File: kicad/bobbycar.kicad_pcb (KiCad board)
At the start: 2 copper layers, 42 x 45 mm, 54 parts, among them J1 IO, J11 CAN2, J12 PROG, J2 IO2, J3 GAS, J4 TFT, J5 Conn_01x04, J7 BREMSE, J8 I2C, J9 CAN3, Q1 SI2301CDS-T1-GE3, U1 ESP32-WROOM-32, U2 TJA1051T-3, U3 MPM2359, U5 MPM2359

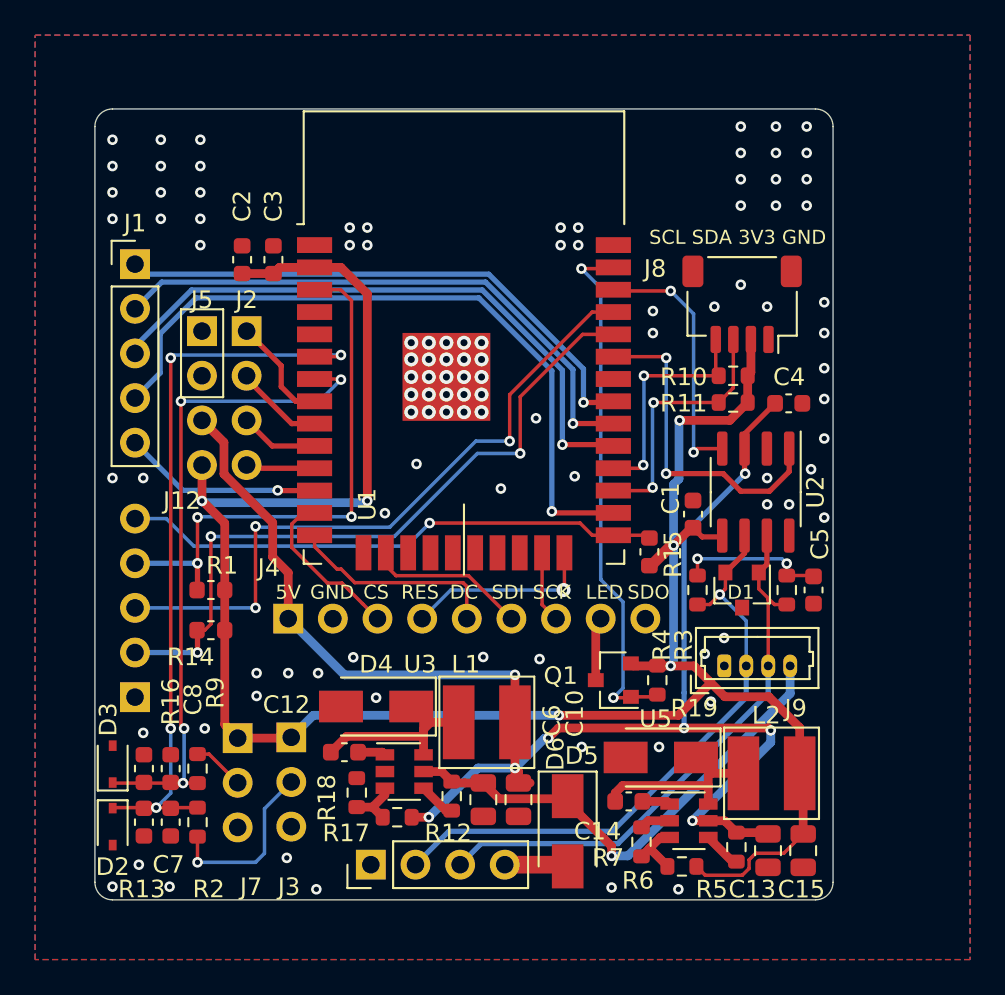
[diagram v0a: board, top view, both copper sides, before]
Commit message: changed to single 3.3V dcdc
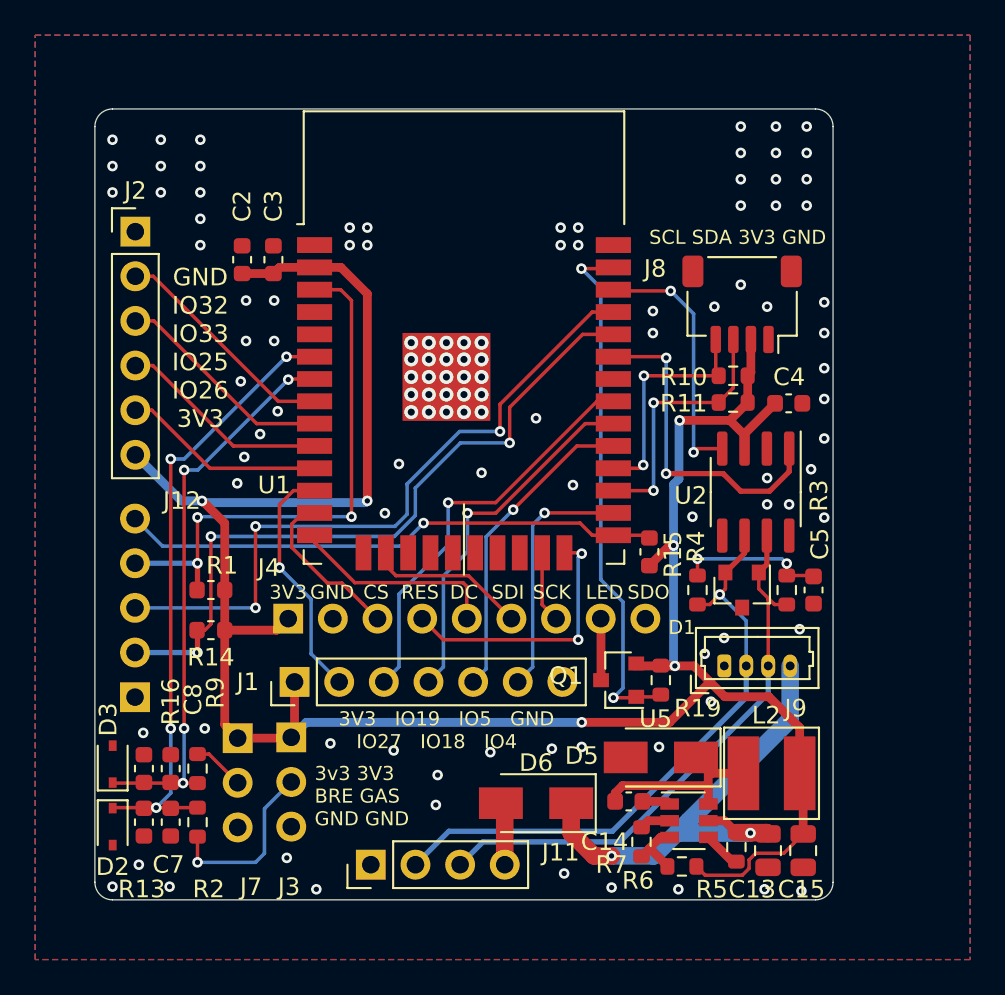
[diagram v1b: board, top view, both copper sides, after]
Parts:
- removed C1: 100n, Capacitor_SMD:C_0603_1608Metric
- removed C10, C6: 22uF, Capacitor_SMD:C_0805_2012Metric
- removed C12: 10n, Capacitor_SMD:C_0603_1608Metric
- removed D4: B230A, Diode_SMD:D_SMA
- removed J5: Conn_01x04, Connector_PinHeader_2.54mm:PinHeader_1x04_P2.54mm_Vertical
- removed L1: 4.7uH, boardcomputer:L_5040
- removed R12: 1k, Resistor_SMD:R_0603_1608Metric
- removed R17: 49.9k, Resistor_SMD:R_0603_1608Metric
- removed R18: 9.53k, Resistor_SMD:R_0603_1608Metric
- removed U3: MPM2359, Package_TO_SOT_SMD:SOT-23-6
- J1: footprint Connector_PinHeader_2.54mm:PinHeader_1x05_P2.54mm_Vertical -> Connector_PinHeader_2.54mm:PinHeader_1x07_P2.54mm_Vertical
- J2: footprint Connector_PinHeader_2.54mm:PinHeader_1x04_P2.54mm_Vertical -> Connector_PinHeader_2.54mm:PinHeader_1x06_P2.54mm_Vertical
- U2: value TJA1051T-3 -> SN65HVD231
- moved J1 25.4 mm to (106.4, 60.6), turned to 90 degrees
- moved J2 8.49 mm to (97.3, 35.0)
- moved D6 2.41 mm to (120.1, 67.5), turned to 180 degrees
- moved Q1 0.30 mm to (124.8, 60.5)
- moved R19 0.20 mm to (127.2, 60.5)
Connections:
- C13 pad 2: +5V -> 15V
- C4 pad 1: +5V -> +3V3
- J1 pad 1: IO19 -> +3V3
- J1 pad 2: IO18 -> IO27
- J1 pad 3: IO5 -> IO19
- J1 pad 4: IO4 -> IO18
- J1 pad 5: IO27 -> IO5
- J2 pad 1: IO32 -> GND
- J2 pad 2: IO33 -> IO32
- J2 pad 3: IO25 -> IO33
- J2 pad 4: IO26 -> IO25
- J4 pad 1: +5V -> +3V3
- R5 pad 2: +5V -> 15V
- U2 pad 3: +5V -> +3V3
- U2 pad 5: +3V3 -> (no net)
- U5 pad 5: +5V -> 15V
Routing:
- net +5V: track 90.2 -> 0.00 mm, vias 8 -> 0
- net IO4: track 40.6 -> 14.2 mm
- net IO5: track 35.1 -> 17.9 mm
- net IO18: track 33.0 -> 20.9 mm
- net Net-(C12-Pad1): track 10.9 -> 0.00 mm
- net +3V3: track 129.3 -> 137.9 mm
- net IO19: track 31.6 -> 23.5 mm
- net IO25: track 4.57 -> 12.2 mm
- net IO26: track 3.94 -> 11.6 mm
- net IO33: track 5.09 -> 12.6 mm
- net IO32: track 6.22 -> 13.1 mm
- net RAW_GAS: track 42.1 -> 35.6 mm
- net RAW_BREMSE: track 38.0 -> 32.5 mm
- net TFT_RESET: track 10.9 -> 15.4 mm, vias 1 -> 2
- net Net-(R17-Pad1): track 3.08 -> 0.00 mm
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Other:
- board text added: "3V3"
- board text added: "3V3 IO19 IO5 GND"
- board text added: "3v3 3V3 BRE GAS GND GND"
- board text added: "GND IO32 IO33 IO25 IO26 3V3"
- board text added: "IO27 IO18 IO4"
- board text removed: "3v3 3V3 GAS BRE GND GND"
- board text removed: "5V"
- board text removed: "GND GND 5V 3V3"
- board text removed: "IO19 IO18 IO5 IO4 IO27"
- board text removed: "IO32 IO33 IO25 IO26"

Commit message: added new CAN connector, added diode matrix
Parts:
- J11: footprint Connector_PinHeader_2.54mm:PinHeader_1x04_P2.54mm_Vertical -> Connector_JST:JST_XH_B4B-XH-A_1x04_P2.50mm_Vertical
- moved D6 2.51 mm to (119.9, 65.0)
- moved J11 1.62 mm to (110.7, 69.4), turned to 0 degrees
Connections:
- J2 pad 1: GND -> +3V3
- J2 pad 6: +3V3 -> GND
- J4 pad 9: (no net) -> TFT_MISO
- U1 pad 17: (no net) -> unconnected-(U1-Pad17)
- U1 pad 18: (no net) -> unconnected-(U1-Pad18)
- U1 pad 19: (no net) -> unconnected-(U1-Pad19)
- U1 pad 20: (no net) -> unconnected-(U1-Pad20)
- U1 pad 21: (no net) -> unconnected-(U1-Pad21)
- U1 pad 22: (no net) -> unconnected-(U1-Pad22)
- U1 pad 32: (no net) -> unconnected-(U1-Pad32)
- U1 pad 4: (no net) -> IO36
- U1 pad 5: (no net) -> IO39
- U2 pad 5: (no net) -> unconnected-(U2-Pad5)
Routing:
- net 15V: track 28.9 -> 31.5 mm
- net Net-(D6-Pad2): track 3.59 -> 4.50 mm
- net GND: vias 110 -> 106
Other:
- net class Default removed

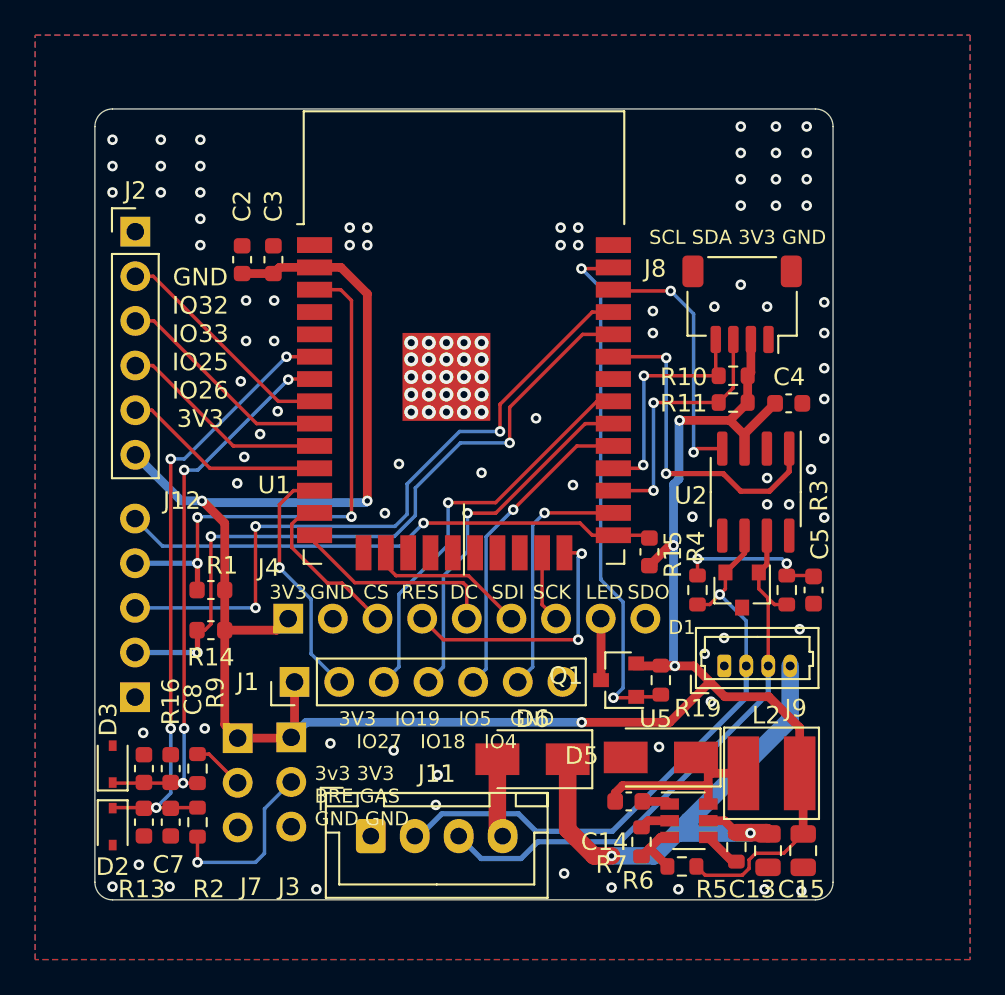
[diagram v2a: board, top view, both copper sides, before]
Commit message: added 16 buttons
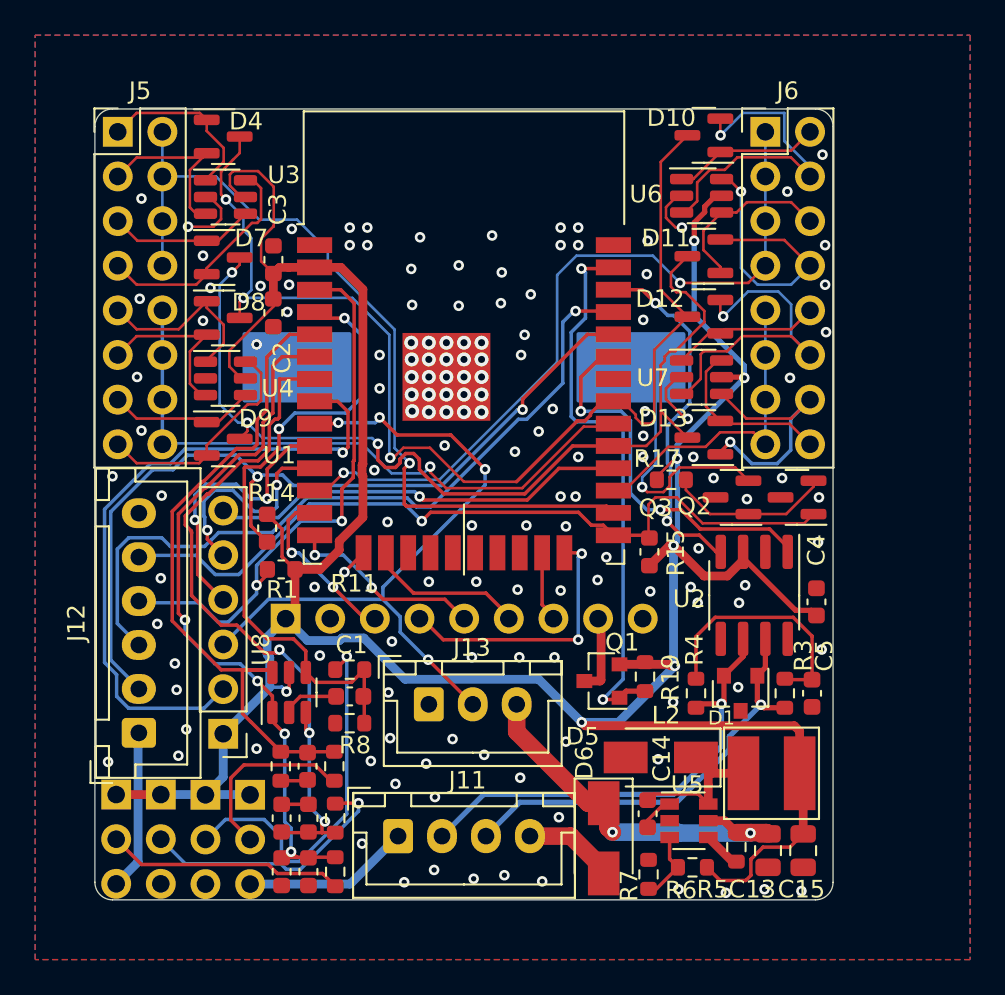
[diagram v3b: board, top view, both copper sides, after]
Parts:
- removed D2, D3: CDSOD323, Diode_SMD:D_SOD-323
- removed J1: IO, Connector_PinHeader_2.54mm:PinHeader_1x07_P2.54mm_Vertical
- removed J9: CAN3, Connector_Molex:Molex_PicoBlade_53047-0410_1x04_P1.25mm_Vertical
- added BZ1: Buzzer, Capacitor_SMD:CP_Elec_18x22, B.Cu at (116.0, 42.7)
- added C1: 100n, Capacitor_SMD:C_0603_1608Metric, F.Cu at (109.5, 61.4)
- added C6: 100n, Capacitor_SMD:C_0603_1608Metric, F.Cu at (107.1, 65.4)
- added D10: BAV99, Package_TO_SOT_SMD:SOT-23, F.Cu at (129.7, 29.5)
- added D11: BAV99, Package_TO_SOT_SMD:SOT-23, F.Cu at (129.7, 36.4)
- added D12: BAV99, Package_TO_SOT_SMD:SOT-23, F.Cu at (129.7, 39.8)
- added D13: BAV99, Package_TO_SOT_SMD:SOT-23, F.Cu at (129.7, 46.7)
- added D4: BAV99, Package_TO_SOT_SMD:SOT-23, F.Cu at (102.3, 29.6)
- added D7: BAV99, Package_TO_SOT_SMD:SOT-23, F.Cu at (102.3, 36.5)
- added D8: BAV99, Package_TO_SOT_SMD:SOT-23, F.Cu at (102.3, 39.9)
- added D9: BAV99, Package_TO_SOT_SMD:SOT-23, F.Cu at (102.3, 46.8)
- added J10: BREMSE, Connector_PinHeader_2.54mm:PinHeader_1x03_P2.54mm_Vertical, F.Cu at (103.8, 67.0)
- added J13: LED, Connector_JST:JST_XH_B3B-XH-A_1x03_P2.50mm_Vertical, F.Cu at (114.0, 61.9)
- added J5: Conn_02x08_Odd_Even, Connector_PinHeader_2.54mm:PinHeader_2x08_P2.54mm_Vertical, F.Cu at (96.3, 29.3)
- added J6: Conn_02x08_Odd_Even, Connector_PinHeader_2.54mm:PinHeader_2x08_P2.54mm_Vertical, F.Cu at (133.2, 29.3)
- added Q2: SI2301CDS-T1-GE3, Package_TO_SOT_SMD:SOT-23, F.Cu at (134.9, 50.1)
- added Q3: SI2301CDS-T1-GE3, Package_TO_SOT_SMD:SOT-23, F.Cu at (131.2, 50.1)
- added R12: 100r, Resistor_SMD:R_0603_1608Metric, F.Cu at (108.6, 65.4)
- added R17: 1k, Resistor_SMD:R_0603_1608Metric, F.Cu at (127.8, 49.1)
- added R8: 100k, Resistor_SMD:R_0603_1608Metric, F.Cu at (109.5, 62.9)
- added U3: USBLC6-4SC6, Package_TO_SOT_SMD:SOT-23-6, F.Cu at (102.4, 33.0)
- added U4: USBLC6-4SC6, Package_TO_SOT_SMD:SOT-23-6, F.Cu at (102.4, 43.3)
- added U6: USBLC6-4SC6, Package_TO_SOT_SMD:SOT-23-6, F.Cu at (129.5, 32.9)
- added U7: USBLC6-4SC6, Package_TO_SOT_SMD:SOT-23-6, F.Cu at (129.5, 43.3)
- added U8: USBLC6-4SC6, Package_TO_SOT_SMD:SOT-23-6, F.Cu at (106.0, 61.2)
- J12: footprint Connector_PinHeader_2.54mm:PinHeader_1x05_P2.54mm_Vertical -> Connector_JST:JST_XH_B6B-XH-A_1x06_P2.50mm_Vertical
- J8: value I2C -> GAS; footprint Connector_JST:JST_SH_SM04B-SRSS-TB_1x04-1MP_P1.00mm_Horizontal -> Connector_PinHeader_2.54mm:PinHeader_1x03_P2.54mm_Vertical
- R10: value 2k2 -> 100k
- R11: value 2k2 -> 100r
- R13, R16: value 1k -> 100k
- moved J8 41.4 mm to (101.3, 67.0), turned to 0 degrees
- moved R10 34.0 mm to (105.6, 65.4), turned to -90 degrees
- moved J2 29.0 mm to (102.3, 63.5), turned to 180 degrees
- moved R11 26.6 mm to (109.5, 59.9), turned to 180 degrees
- moved C4 11.4 mm to (136.1, 56.0), turned to 90 degrees
- moved J3 10.5 mm to (96.2, 67.0)
- moved C7 8.33 mm to (107.2, 71.4)
- moved C8 8.33 mm to (107.2, 68.4)
- moved R2 8.33 mm to (108.7, 71.4)
- moved R9 8.33 mm to (108.7, 68.4)
- moved R13 8.33 mm to (105.6, 71.4)
- moved R16 8.33 mm to (105.6, 68.4)
- moved R14 6.63 mm to (104.8, 51.9), turned to 90 degrees
- moved D6 6.05 mm to (124.0, 69.5), turned to -90 degrees
- moved R3 5.88 mm to (134.3, 61.2)
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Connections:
- J2 pad 6: GND -> IO17
- J8 pad 1: GND -> +3V3
- J8 pad 2: +3V3 -> Net-(J8-Pad2)
- J8 pad 3: SDA -> GND
- R10 pad 1: SCL -> RAW_M365_BREMS
- R10 pad 2: +3V3 -> GND
- R11 pad 1: SDA -> RAW_M365_GAS
- R11 pad 2: +3V3 -> Net-(J8-Pad2)
- U1 pad 12: IO27 -> IN3
- U1 pad 26: IO4 -> IN1
- U1 pad 27: SDA -> IN4
- U1 pad 28: SCL -> IO17
- U1 pad 30: IO18 -> IN2
- U1 pad 4: IO36 -> RAW_M365_GAS
- U1 pad 5: IO39 -> RAW_M365_BREMS
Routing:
- net IN1: track 0.00 -> 47.4 mm, vias 0 -> 1
- net IN3: track 0.00 -> 43.1 mm, vias 0 -> 2
- net IO19: track 23.5 -> 64.9 mm, vias 1 -> 3
- net RAW_M365_BREMS: track 0.00 -> 38.2 mm
- net IO5: track 17.9 -> 55.1 mm, vias 1 -> 3
- net RAW_M365_GAS: track 0.00 -> 36.6 mm, vias 0 -> 2
- net IN2: track 0.00 -> 36.3 mm, vias 0 -> 1
- net GND: track 1.76 -> 36.7 mm, vias 106 -> 145
- net +3V3: track 137.9 -> 172.2 mm, vias 6 -> 7
- net IO33: track 12.6 -> 39.2 mm, vias 0 -> 4
- net IO32: track 13.1 -> 37.4 mm, vias 0 -> 1
- net IO17: track 0.00 -> 23.9 mm, vias 0 -> 1
- net Net-(J8-Pad2): track 0.00 -> 21.2 mm, vias 0 -> 1
- net IO18: track 20.9 -> 0.00 mm, vias 1 -> 0
- net B14: track 0.00 -> 19.0 mm, vias 0 -> 1
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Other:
- board text added: "15V D+ D- GND"
- board text added: "15V LED GND"
- board text added: "3v3 3V3 3V3 3V3 BRE3 GAS3 BRE GAS GND GND GND GND"
- board text added: "Analog"
- board text added: "CAN"
- board text added: "Flash"
- board text added: "GPIO"
- board text added: "IO17 IO26 IO25 IO33 IO32 3V3"
- board text added: "IO33"
- board text added: "TFT"
- board text added: "VIN IO0 EN TX RX GND"
- board text removed: "3V3 IO19 IO5 GND"
- board text removed: "3v3 3V3 BRE GAS GND GND"
- board text removed: "GND CANL CANH 15V"
- board text removed: "GND IO32 IO33 IO25 IO26 3V3"
- board text removed: "IO0 EN TX RX GND"
- board text removed: "IO27 IO18 IO4"
- board text removed: "SCL SDA 3V3 GND"

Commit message: ordered at jlcpcb
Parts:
- removed Q2, Q3: SI2301CDS-T1-GE3, Package_TO_SOT_SMD:SOT-23
- removed R17: 1k, Resistor_SMD:R_0603_1608Metric
- added C10: 1u, Resistor_SMD:R_0805_2012Metric, F.Cu at (133.3, 50.2)
- added D14: D, Diode_SMD:D_SOD-123, F.Cu at (128.4, 56.4)
- added JP1: Jumper_2_Open, Jumper:SolderJumper-2_P1.3mm_Open_RoundedPad1.0x1.5mm, B.Cu at (135.1, 50.4)
- added R21: 4.7k, Resistor_SMD:R_0603_1608Metric, F.Cu at (135.3, 50.2)
- added U9: MCP1416, Package_TO_SOT_SMD:SOT-23-5, F.Cu at (129.9, 50.2)
- moved C4 2.15 mm to (136.1, 58.2), turned to -90 degrees
- turned BZ1 to 0 degrees
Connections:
- BZ1 pad 1: BUZZER -> 15V
- BZ1 pad 2: GND -> BUZZER
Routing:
- net 15V: track 21.8 -> 96.5 mm, vias 2 -> 6
- net Net-(D14-Pad2): track 0.00 -> 39.7 mm, vias 0 -> 4
- net Net-(Q2-Pad2): track 9.40 -> 0.00 mm
- net IO0: track 44.7 -> 35.9 mm
- net GND: track 36.7 -> 44.0 mm, vias 145 -> 155
- net CAN_TX: track 21.9 -> 27.9 mm, vias 2 -> 4
- net Net-(C10-Pad1): track 0.00 -> 5.76 mm, vias 0 -> 1
- net BUZZER: track 15.1 -> 17.5 mm, vias 1 -> 2
- net TFT_RESET: track 15.4 -> 13.4 mm
- net Net-(C5-Pad1): track 14.0 -> 12.5 mm
- net RAW_M365_GAS: track 36.6 -> 37.9 mm
- net +3V3: track 172.2 -> 172.5 mm, vias 7 -> 6
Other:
- board text added: "DC speaker"
